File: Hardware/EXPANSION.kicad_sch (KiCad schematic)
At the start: 1 part, among them J5 Screw_Terminal_01x08

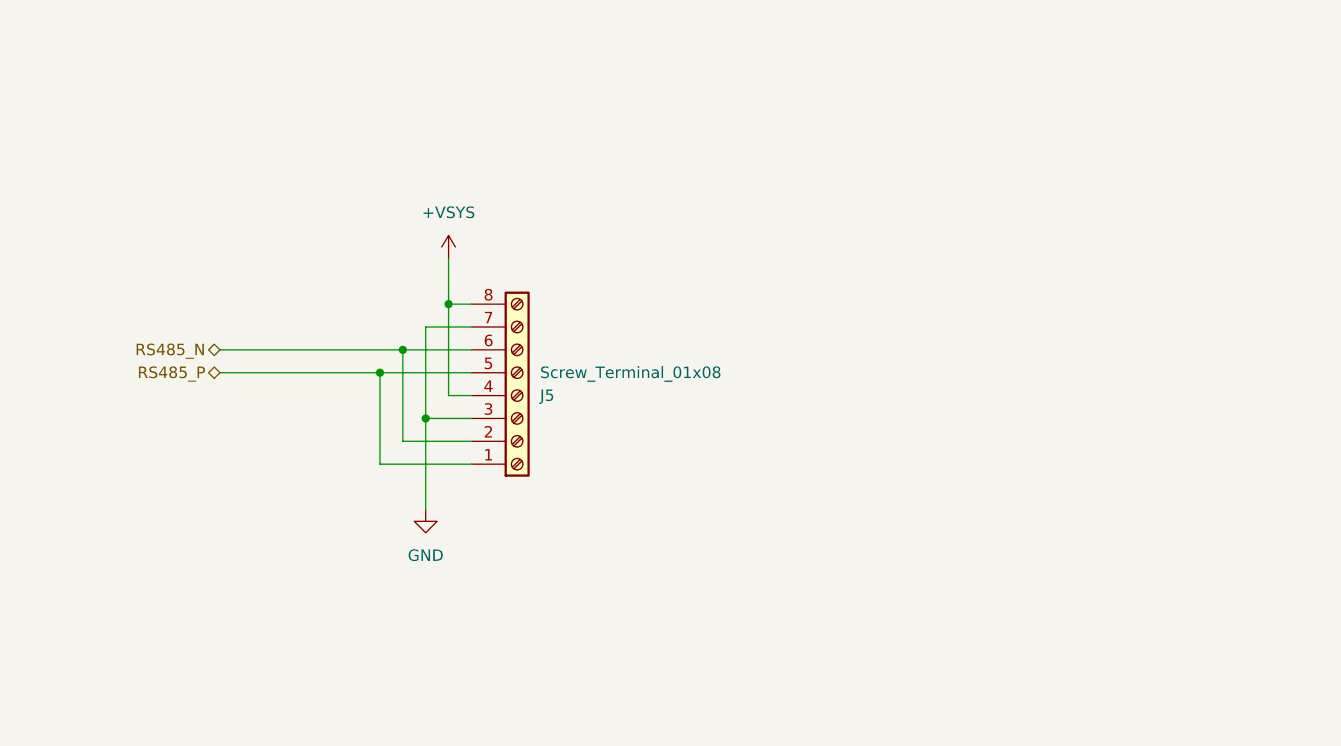
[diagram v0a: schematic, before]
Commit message: remove unused sheets
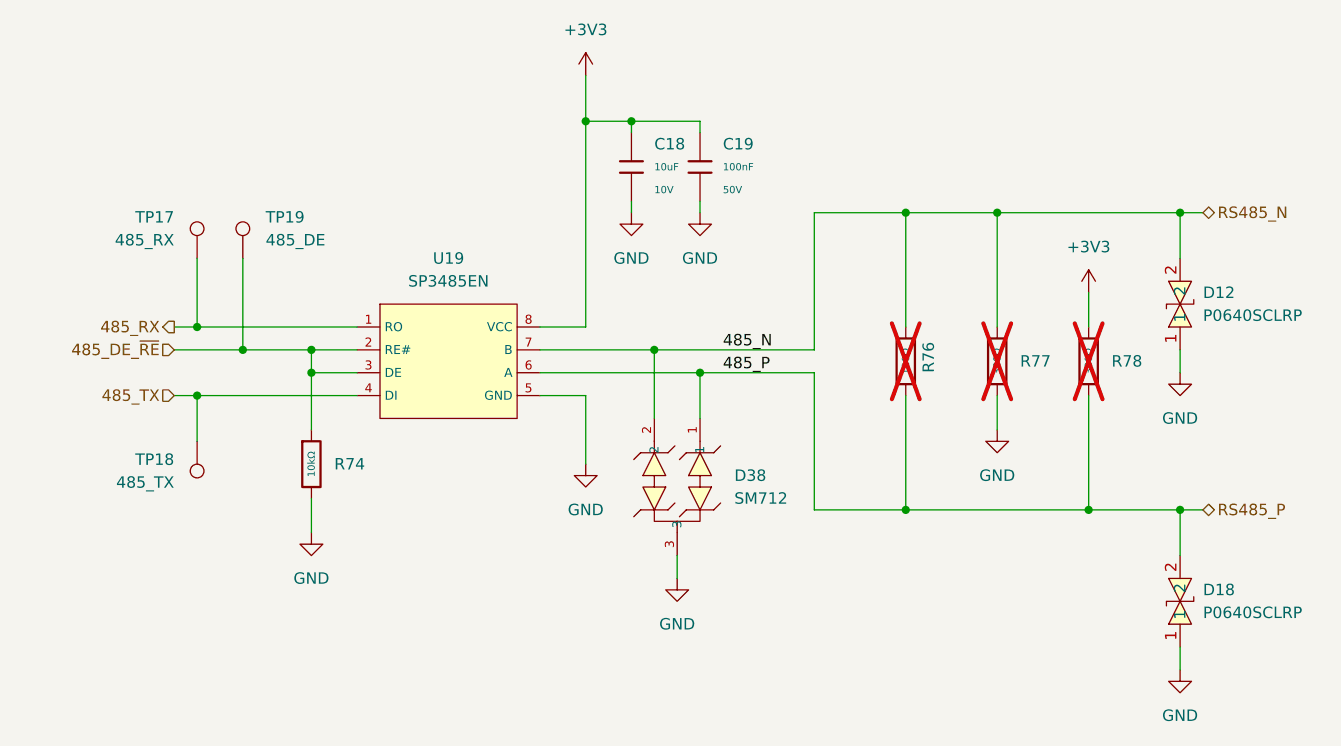
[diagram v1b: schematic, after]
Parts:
- removed J5: Screw_Terminal_01x08, TerminalBlock:TerminalBlock_MaiXu_MX126-5.0-08P_1x08_P5.00mm, symbol Connector:Screw_Terminal_01x08
- added C18: 10uF, PCM_JLCPCB:C_0603, symbol PCM_JLCPCB-Capacitors:0603,10uF
- added C19: 100nF, PCM_JLCPCB:C_0603, symbol PCM_JLCPCB-Capacitors:0603,100nF
- added D12, D18: P0640SCLRP, EasyEDA:SMB_L4.6-W3.6-LS5.3-BI, symbol EasyEDA:P0640SCLRP
- added D38: SM712, PCM_JLCPCB:SOT-23-3_L2.9-W1.3-P1.90-LS2.4-BR, symbol PCM_JLCPCB-Diode-Packages:TVS-Bi, SM712
- added R74: 10kΩ, PCM_JLCPCB:R_0603, symbol PCM_JLCPCB-Resistors:0603,10kΩ
- added R76: 120Ω, PCM_JLCPCB:R_0805, symbol PCM_JLCPCB-Resistors:0805,120Ω
- added R77, R78: 330Ω, PCM_JLCPCB:R_0603, symbol PCM_JLCPCB-Resistors:0603,330Ω
- added TP17: 485_RX, TestPoint:TestPoint_Pad_D1.0mm, symbol Connector:TestPoint
- added TP18: 485_TX, TestPoint:TestPoint_Pad_D1.0mm, symbol Connector:TestPoint
- added TP19: 485_DE, TestPoint:TestPoint_Pad_D1.0mm, symbol Connector:TestPoint
- added U19: SP3485EN, PCM_JLCPCB:SOIC-8_L5.0-W4.0-P1.27-LS6.0-BL, symbol PCM_JLCPCB-Interface:Transceiver, RS485/422, 10Mbps, SP3485EN-L/TR
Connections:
- net GND: now also C18.2, C19.2, D12.1, D18.1, D38.3, R74.2, R77.2, U19.5 (GND)
- net RS485_N: now also D12.2, D38.2, R76.1, R77.1, U19.7 (B)
- net RS485_P: now also D18.2, D38.1, R76.2, R78.2, U19.6 (A)
- new net +3V3: C18.1, C19.1, R78.1, U19.8 (VCC)
- new net 485_DE_~{RE}: R74.1, TP19.1, U19.2 (RE#), U19.3 (DE)
- new net 485_RX: TP17.1, U19.1 (RO)
- new net 485_TX: TP18.1, U19.4 (DI)
